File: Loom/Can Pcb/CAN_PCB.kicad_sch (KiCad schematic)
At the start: 11 parts, among them J1 Screw_Terminal_01x02, J2 Conn_01x05_Pin, J3 Screw_Terminal_01x02, J4 Screw_Terminal_01x02, U2 MCP2551-I-SN, U3 TL780-05KCS, Y1 Crystal

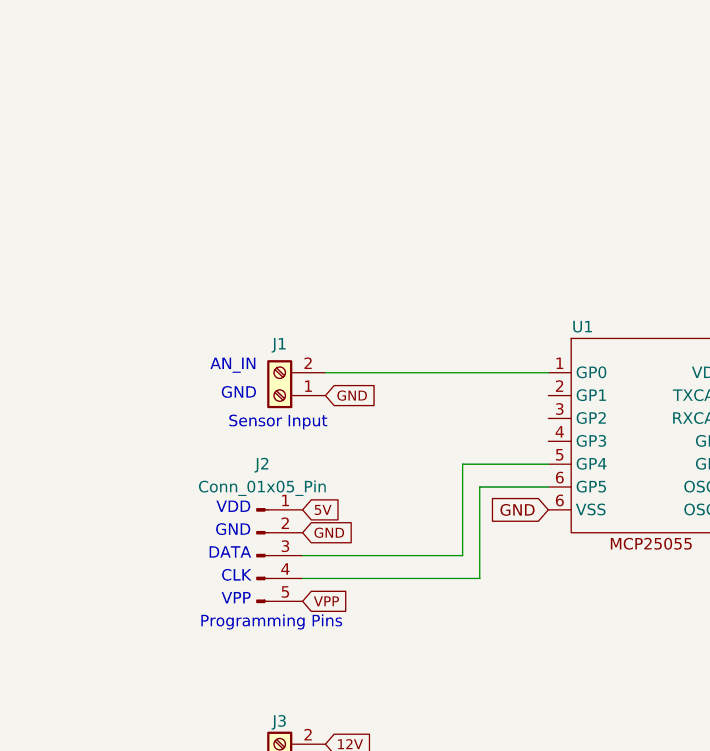
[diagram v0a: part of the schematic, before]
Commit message: Added the addional inputs to the schematic
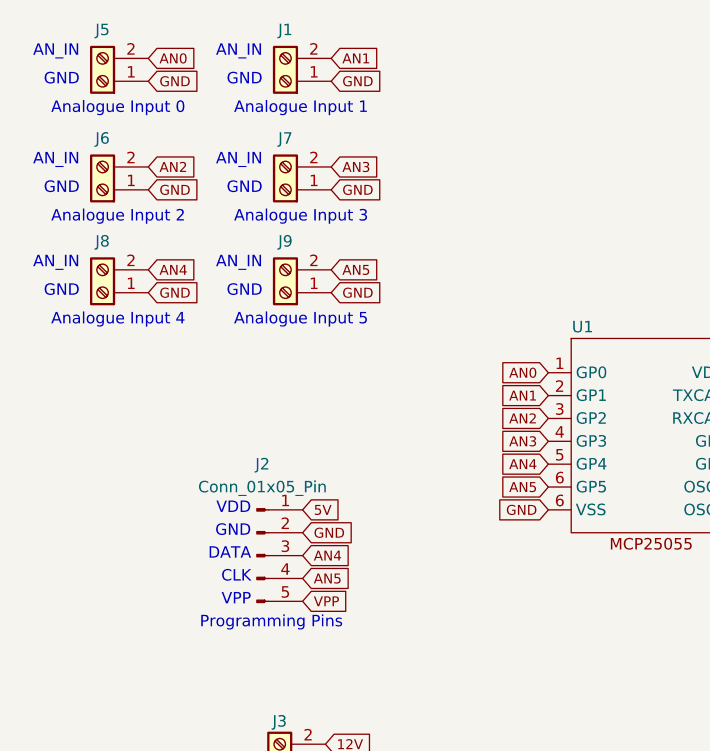
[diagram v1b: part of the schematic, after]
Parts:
- added J5, J6, J7, J8, J9: Screw_Terminal_01x02, symbol Connector:Screw_Terminal_01x02
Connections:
- net GND: now also J5.1 (Pin_1), J6.1 (Pin_1), J7.1 (Pin_1), J8.1 (Pin_1), J9.1 (Pin_1)
- net AN4: now reaches J2.3 (Pin_3), U1.5 (GP4)
- net AN4: now also J8.2 (Pin_2)
- net AN5: now reaches J2.4 (Pin_4), U1.6 (VSS)
- net AN5: now also J9.2 (Pin_2)
- net AN0: now reaches U1.1 (GP0)
- net AN0: now also J5.2 (Pin_2); no longer J1.2 (Pin_2)
- net AN1: now reaches U1.2 (GP1)
- net AN1: now also J1.2 (Pin_2)
- net AN2: now reaches U1.3 (GP2)
- net AN2: now also J6.2 (Pin_2)
- net AN3: now reaches U1.4 (GP3)
- net AN3: now also J7.2 (Pin_2)
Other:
- note added: "Analogue Input 0"
- note added: "Analogue Input 1"
- note added: "Analogue Input 2"
- note added: "Analogue Input 3"
- note added: "Analogue Input 4"
- note added: "Analogue Input 5"
- note removed: "Sensor Input"
- moved on the sheet: J1

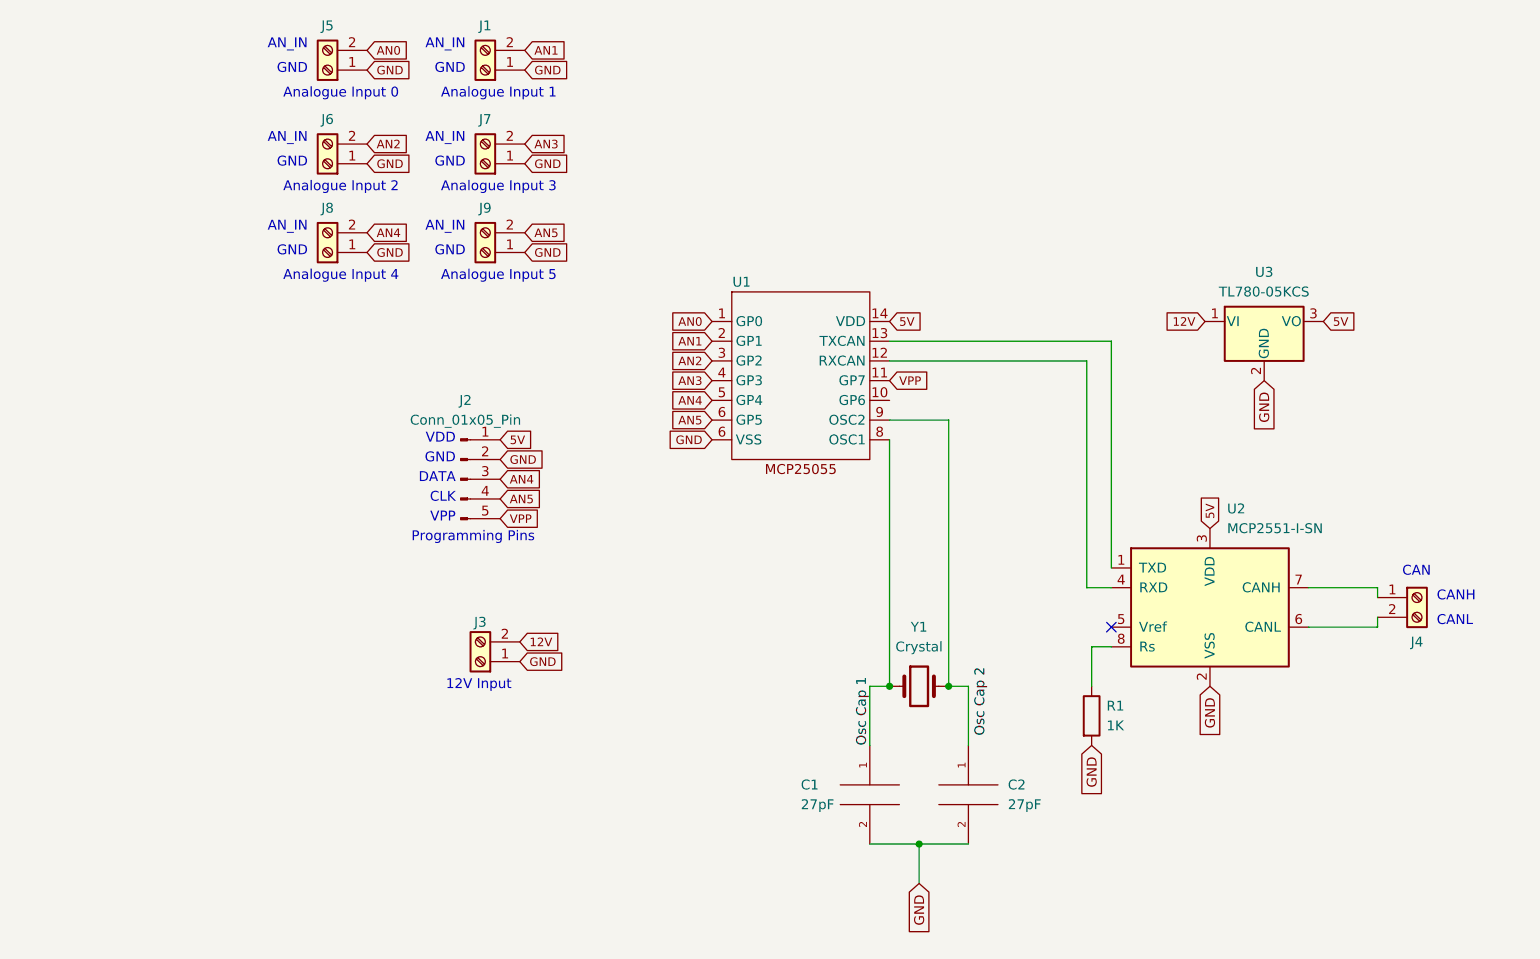
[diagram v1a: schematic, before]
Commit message: CAN PCB initial layout and schematic changes
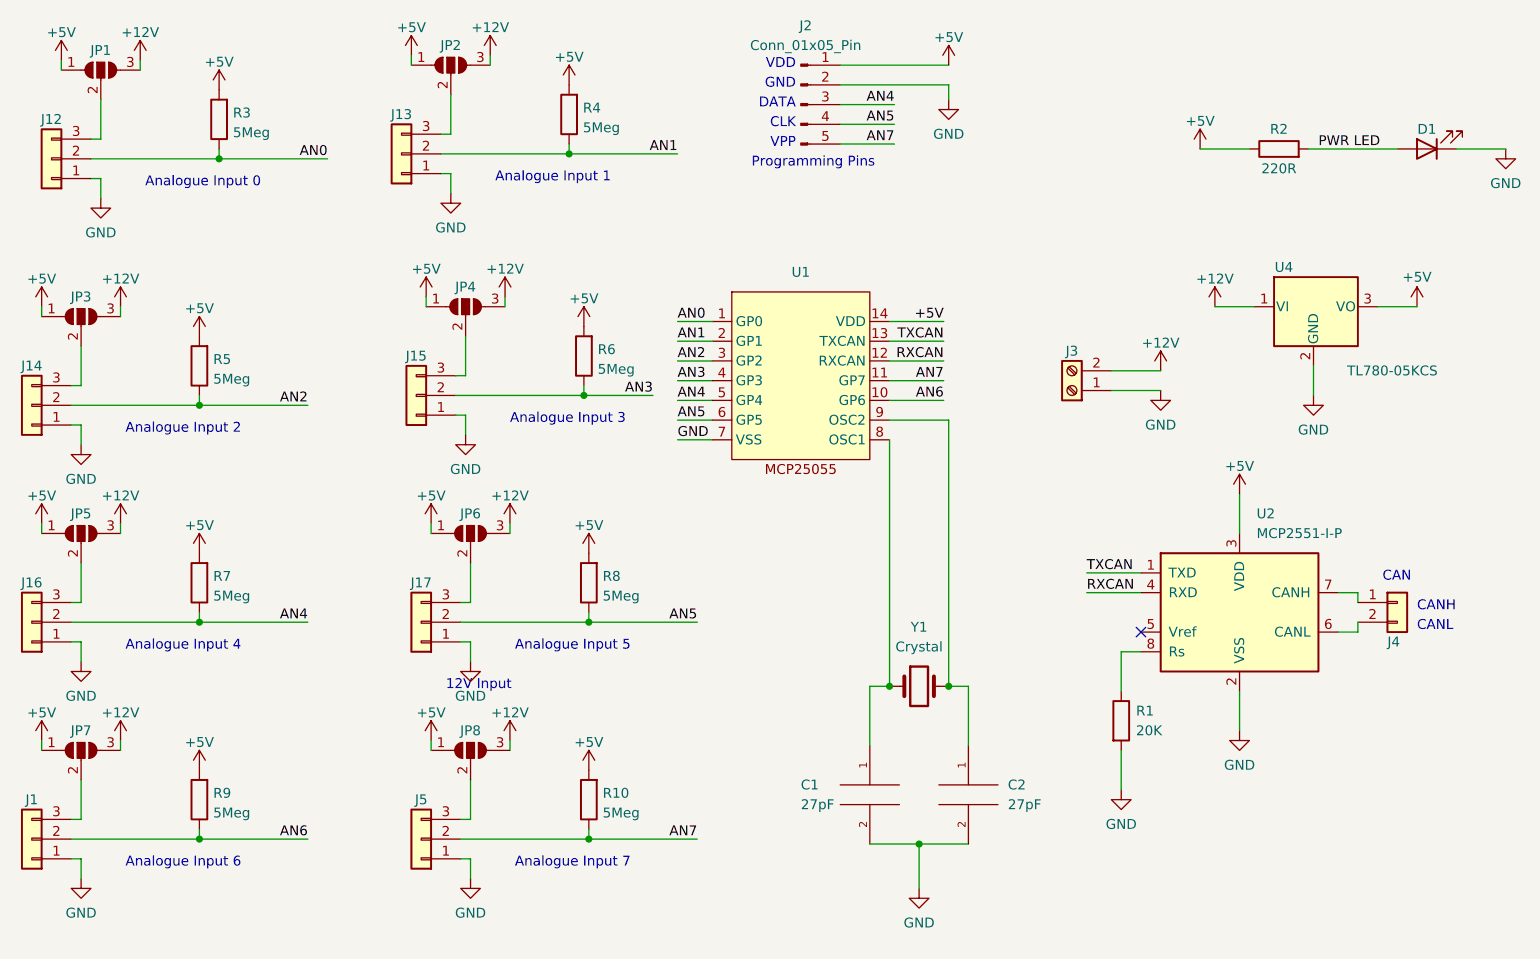
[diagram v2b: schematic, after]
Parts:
- removed J1, J4, J5, J6, J7, J8, J9: Screw_Terminal_01x02, symbol Connector:Screw_Terminal_01x02
- removed U2: MCP2551-I-SN, Package_SO:SOIC-8_3.9x4.9mm_P1.27mm, symbol Interface_CAN_LIN:MCP2551-I-SN
- removed U3: TL780-05KCS, Package_TO_SOT_THT:TO-220-3_Vertical, symbol Regulator_Linear:TL780-05KCS
- added D1: PWR LED, LED_THT:LED_D3.0mm, symbol Device:LED
- added J1, J12, J13, J14, J15, J16, J17, J5: Conn_01x03, BSPD_footprints:ATF13-3P-BM03, symbol Connector_Generic:Conn_01x03
- added J4: Conn_01x02, Footprints:ATF13-2P-BM03, symbol Connector_Generic:Conn_01x02
- added JP1, JP2, JP3, JP4, JP5, JP6, JP7, JP8: SolderJumper_3_Open, Jumper:SolderJumper-3_P1.3mm_Open_Pad1.0x1.5mm, symbol Jumper:SolderJumper_3_Open
- added R10, R3, R4, R5, R6, R7, R8, R9: 5Meg, Resistor_THT:R_Axial_DIN0207_L6.3mm_D2.5mm_P7.62mm_Horizontal, symbol Device:R
- added R2: 220R, Resistor_THT:R_Axial_DIN0207_L6.3mm_D2.5mm_P7.62mm_Horizontal, symbol Device:R
- added U2: MCP2551-I-P, Package_DIP:DIP-8_W7.62mm_Socket, symbol Interface_CAN_LIN:MCP2551-I-P
- added U4: TL780-05KCS, Package_TO_SOT_THT:TO-220-3_Horizontal_TabDown, symbol Regulator_Linear:TL780-05KCS
- J2: footprint (none) -> Connector_PinHeader_2.54mm:PinHeader_1x05_P2.54mm_Vertical
- J3: footprint (none) -> TerminalBlock:TerminalBlock_bornier-2_P5.08mm
- R1: value 1K -> 20K; footprint (none) -> Resistor_THT:R_Axial_DIN0207_L6.3mm_D2.5mm_P7.62mm_Horizontal
- U1: footprint (none) -> Package_DIP:DIP-14_W7.62mm_Socket
- Y1: footprint Osc:9B-16.000MAAJ-B -> Footprints:9B-16.000MAAJ-B
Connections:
- net AN0: now also J12.2 (Pin_2), R3.1
- net AN1: now also J13.2 (Pin_2), R4.1
- net AN2: now also J14.2 (Pin_2), R5.1
- net AN3: now also J15.2 (Pin_2), R6.1
- net AN4: now also J16.2 (Pin_2), R7.1
- net AN5: now also J17.2 (Pin_2), R8.1
- net GND: now also U1.7 (VSS), D1.1 (K), J1.1 (Pin_1), J12.1 (Pin_1), J13.1 (Pin_1), J14.1 (Pin_1), J15.1 (Pin_1), J16.1 (Pin_1), J17.1 (Pin_1), J5.1 (Pin_1), U2.2 (VSS), U4.2 (GND); no longer U1.6 (VSS)
- net TXCAN: now reaches U1.13 (TXCAN)
- net TXCAN: now also U2.1 (TXD)
- net RXCAN: now reaches U1.12 (RXCAN)
- net RXCAN: now also U2.4 (RXD)
- net at R1.1: now also U2.8 (Rs)
- net AN6: now reaches U1.10 (GP6)
- net AN6: now also J1.2 (Pin_2), R9.1
- net 12V renamed +12V
- net +12V: now also JP1.3 (B), JP2.3 (B), JP3.3 (B), JP4.3 (B), JP5.3 (B), JP6.3 (B), JP7.3 (B), JP8.3 (B), U4.1 (VI)
- net 5V renamed +5V
- net +5V: now also JP1.1 (A), JP2.1 (A), JP3.1 (A), JP4.1 (A), JP5.1 (A), JP6.1 (A), JP7.1 (A), JP8.1 (A), R10.2, R2.1, R3.2, R4.2, R5.2, R6.2, R7.2, R8.2, R9.2, U2.3 (VDD), U4.3 (VO)
- net Osc Cap 1: no longer names the net of C1.1, U1.8 (OSC1), Y1.1
- net VPP renamed AN7
- net AN7: now also J5.2 (Pin_2), R10.1
- new net: J15.3 (Pin_3), JP4.2 (C)
- new net: J14.3 (Pin_3), JP3.2 (C)
- new net: J13.3 (Pin_3), JP2.2 (C)
- new net: J17.3 (Pin_3), JP6.2 (C)
- new net: J5.3 (Pin_3), JP8.2 (C)
- new net: J16.3 (Pin_3), JP5.2 (C)
- new net: J12.3 (Pin_3), JP1.2 (C)
- new net: J1.3 (Pin_3), JP7.2 (C)
- new net: J4.2 (Pin_2), U2.6 (CANL)
- new net: J4.1 (Pin_1), U2.7 (CANH)
- new net PWR LED: D1.2 (A), R2.2
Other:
- note added: "Analogue Input 6"
- note added: "Analogue Input 7"
- note removed: "AN_IN"
- title: (none) -> Can Adapeter PCB
- moved on the sheet: J2, J3, R1

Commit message: Made changes to can pcb layout
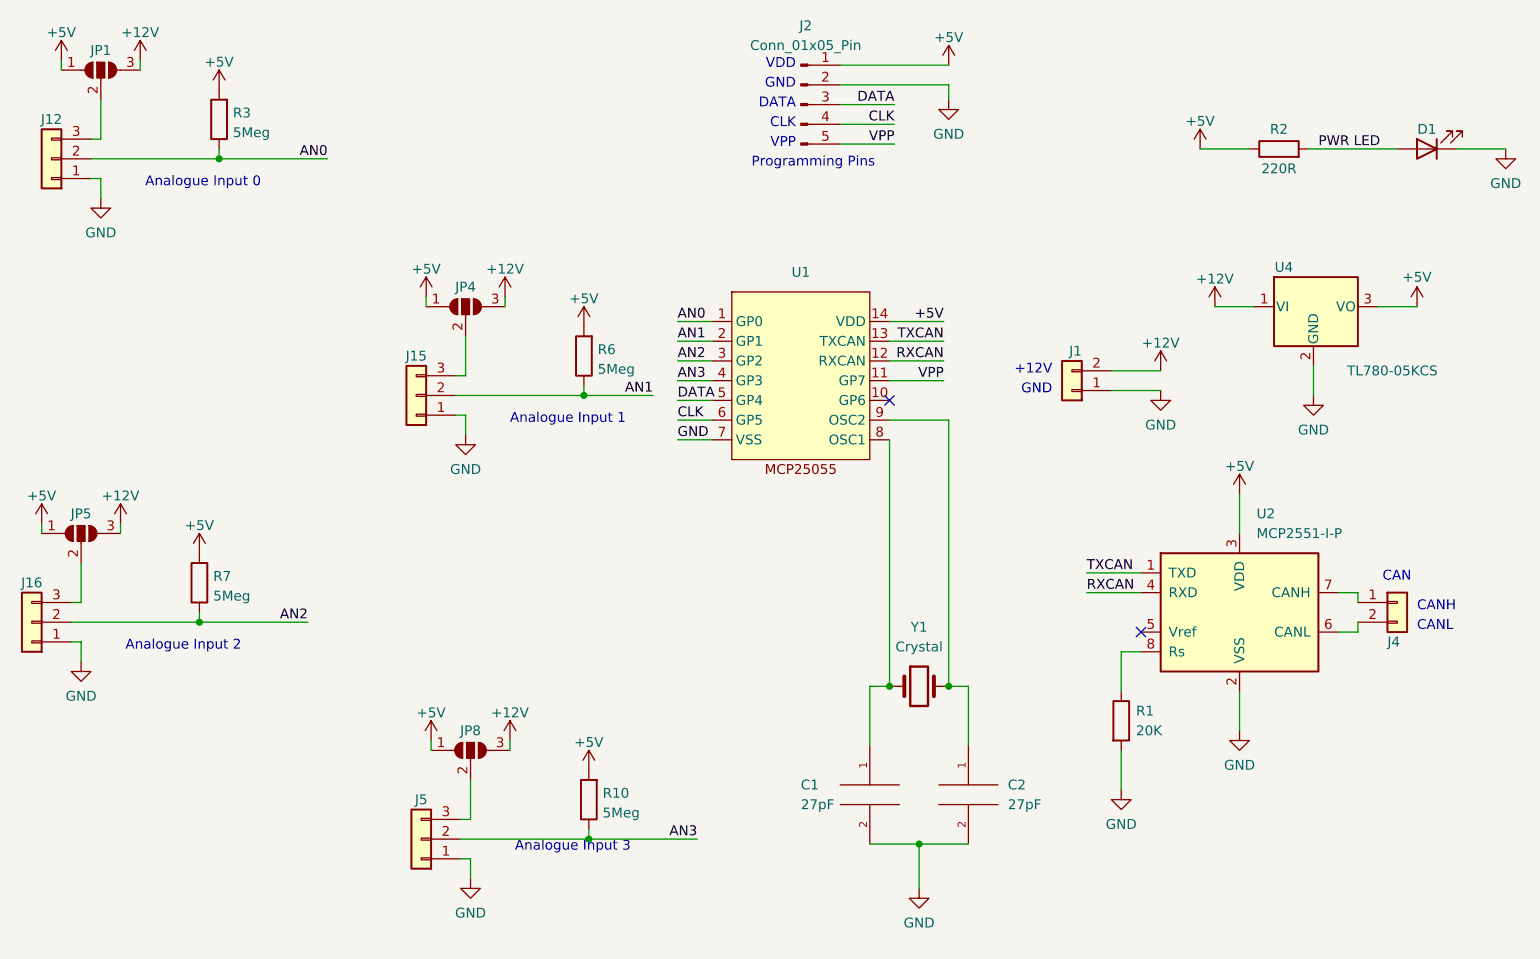
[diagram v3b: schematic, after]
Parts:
- removed J1, J13, J14, J17: Conn_01x03, BSPD_footprints:ATF13-3P-BM03, symbol Connector_Generic:Conn_01x03
- removed J3: Screw_Terminal_01x02, TerminalBlock:TerminalBlock_bornier-2_P5.08mm, symbol Connector:Screw_Terminal_01x02
- removed JP2, JP3, JP6, JP7: SolderJumper_3_Open, Jumper:SolderJumper-3_P1.3mm_Open_Pad1.0x1.5mm, symbol Jumper:SolderJumper_3_Open
- removed R4, R5, R8, R9: 5Meg, Resistor_THT:R_Axial_DIN0207_L6.3mm_D2.5mm_P7.62mm_Horizontal, symbol Device:R
- added J1: Conn_01x02, Footprints:ATF13-2P-BM03, symbol Connector_Generic:Conn_01x02
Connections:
- net +12V: now also J1.2 (Pin_2)
- net AN1: now also J15.2 (Pin_2), R6.1
- net AN2: now also J16.2 (Pin_2), R7.1
- net AN3: now also J5.2 (Pin_2), R10.1; no longer J15.2 (Pin_2), R6.1
- net GND: now also J1.1 (Pin_1)
- net AN4 renamed DATA
- net DATA: no longer J16.2 (Pin_2), R7.1
- net AN5 renamed CLK
- net AN6: no longer names the net of U1.10 (GP6)
- net AN7 renamed VPP
- net VPP: no longer J5.2 (Pin_2), R10.1
- no-connect marks 1 -> 2
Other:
- note added: "+12V"
- note removed: "12V Input"
- note removed: "Analogue Input 4"
- note removed: "Analogue Input 5"
- note removed: "Analogue Input 6"
- note removed: "Analogue Input 7"
